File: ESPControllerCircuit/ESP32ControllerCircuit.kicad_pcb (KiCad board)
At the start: 2 copper layers, 65 x 55 mm, 45 parts, among them J1 I2C, J2 Battery Sense, J3 Inverter/Charger SS Relays, J4 Inverter PWM Control, J5 BST900 Serial, J6 I/O, U1 MAX5033AASA, U2 INA226, U3 Wemos_LoLin32_Lite, U4 HMHA2801

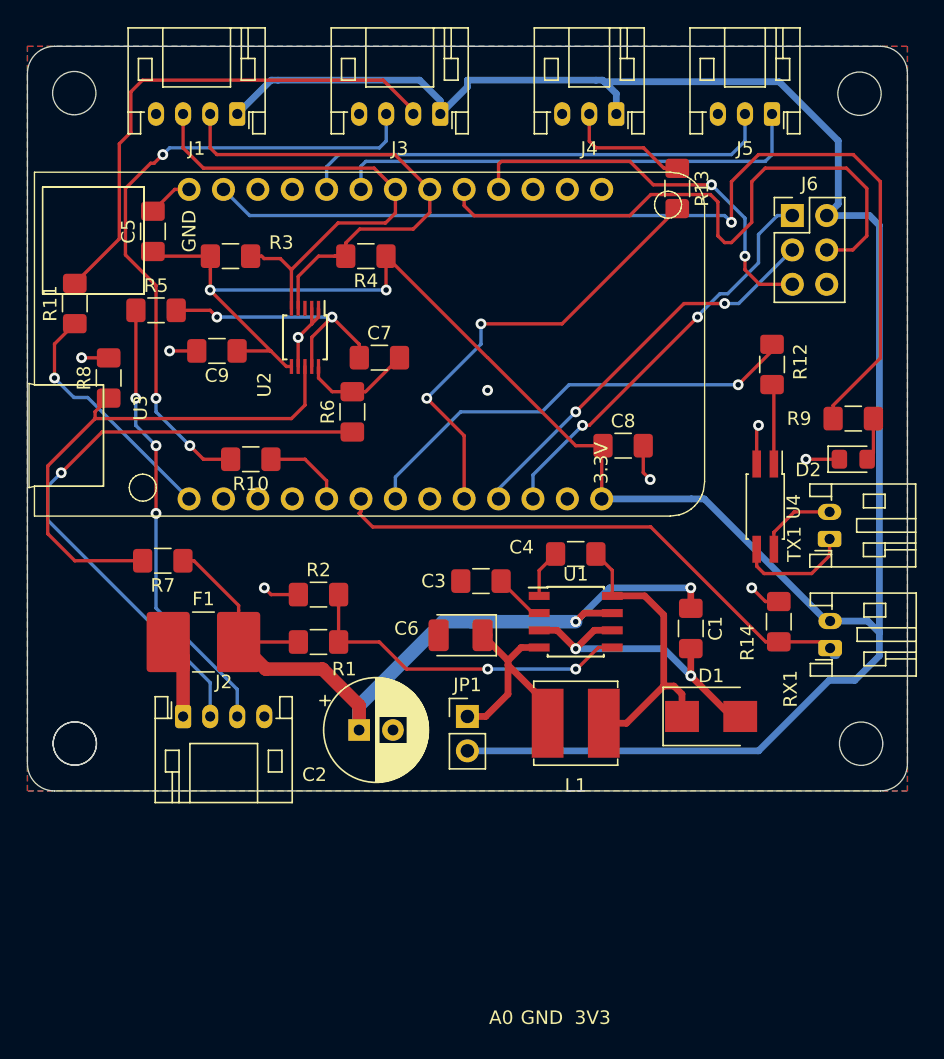
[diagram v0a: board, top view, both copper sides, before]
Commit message: use different pins for I2C
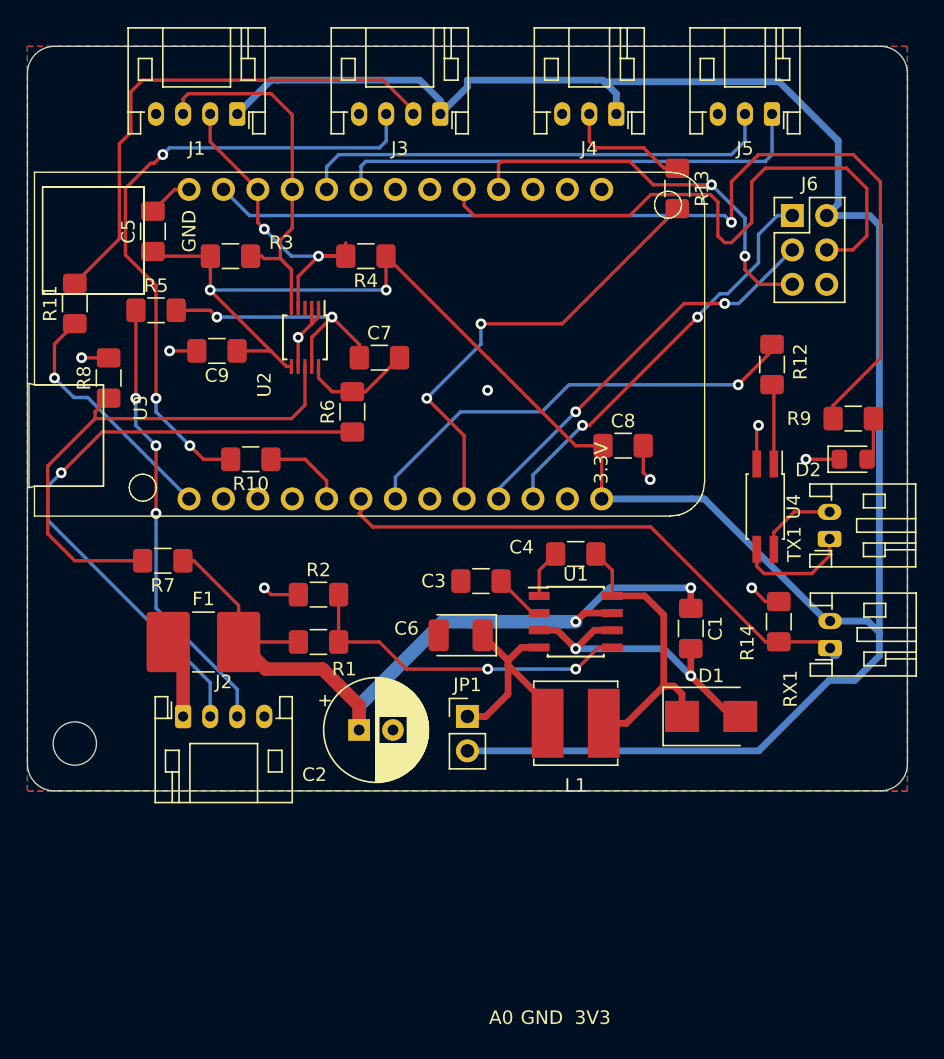
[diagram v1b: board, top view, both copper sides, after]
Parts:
- removed the REF** at (134.1, 128.5)
- removed the REF** at (134.0, 80.5)
- removed the REF** at (76.0, 80.5)
- removed the REF** at (76.0, 128.5)
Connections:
- U3 pad 10: (no net) -> SCL
- U3 pad 11: (no net) -> SDA
- U3 pad 6: SDA -> (no net)
- U3 pad 7: SCL -> (no net)
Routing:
- net SDA: track 37.1 -> 24.8 mm, vias 0 -> 2
- net SCL: track 36.9 -> 27.2 mm
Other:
- board text added: "ESP32 diyBMS Controller ver1.1"
- board text removed: "ESP32 diyBMS Controller"
